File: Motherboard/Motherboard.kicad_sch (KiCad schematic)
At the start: 56 parts, among them J1 Conn_01x01, J10 ATX-24, J11 USB_B, J12 Bus_ISA_8bit, J13 65SIB_Connector, J2 Conn_01x01, J3 Conn_01x01, J4 Conn_01x01, J5 Conn_01x01, J6 Conn_01x01, J7 Conn_01x01, J8 Conn_01x01, J9 Bus_ISA_8bit, SW1 SW_Push, SW2 SW_SPST, U1 SC28L91, U10 XCR3064XL-VQ100, U11 XCR3064-VQ100, U12 LM7905_TO220, U13 MCP2200-I-SO, U14 74HCT163, U15 74HCT137, U2 AS6C1608, U3 WD65C22, U4 SST39SF040, U5 SST39SF040, U6 WD65C816S, U7 DS1813, U8 74HCT245, U9 74HCT573, X1 ACO-3.6864MHz, X2 ACO-24MHz, X3 ACO-14.31818MHz

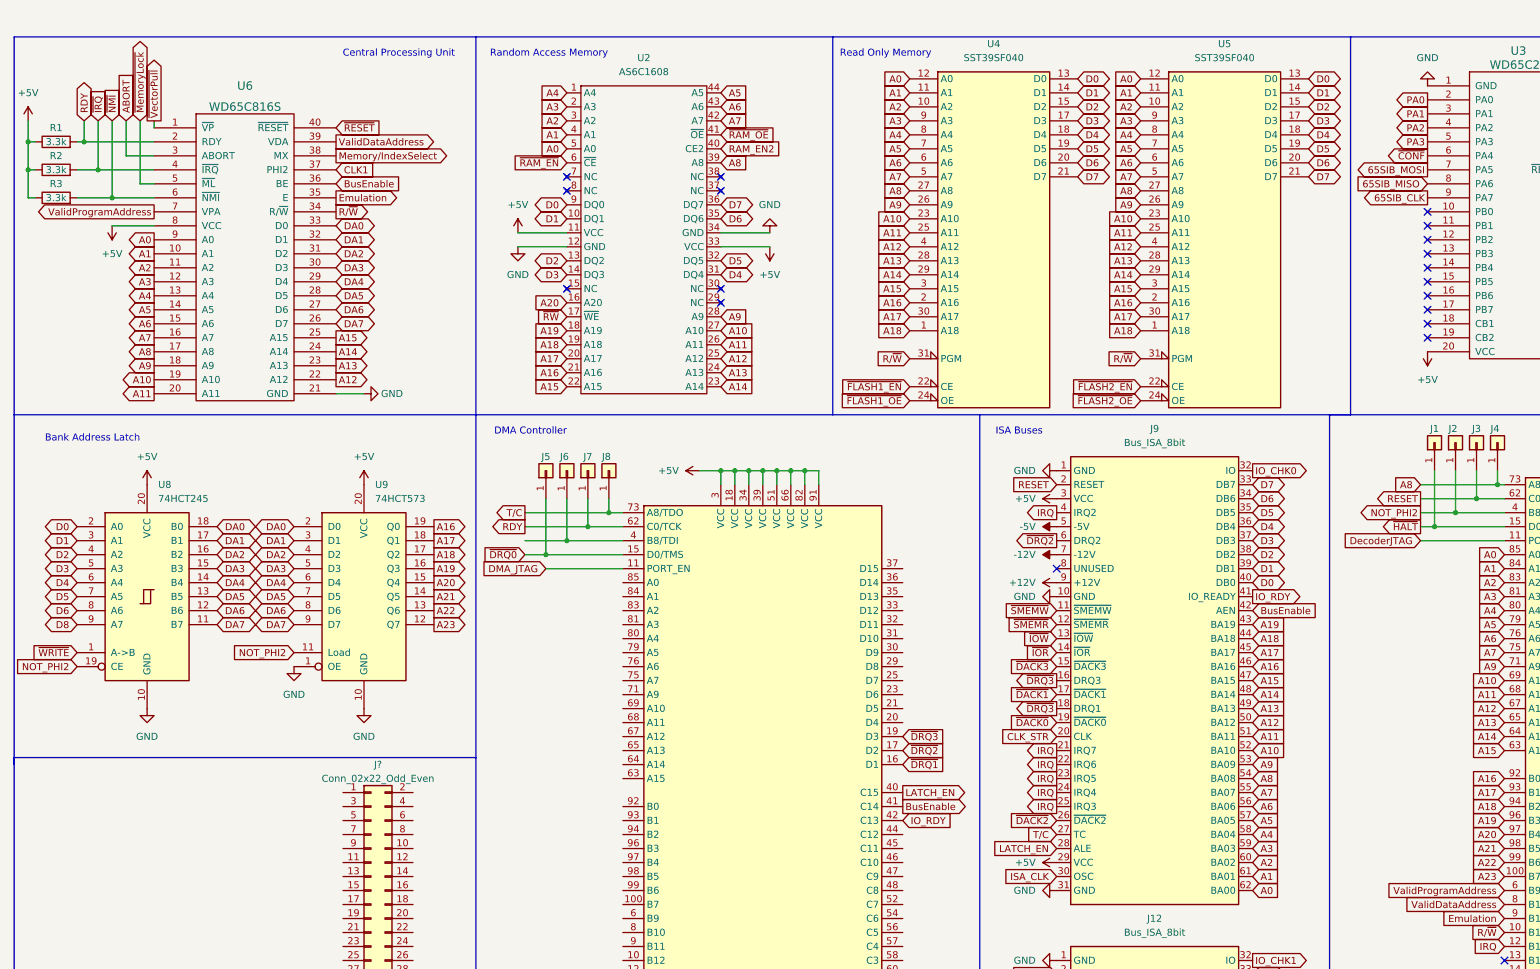
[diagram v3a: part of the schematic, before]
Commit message: Update Motherboard.kicad_sch
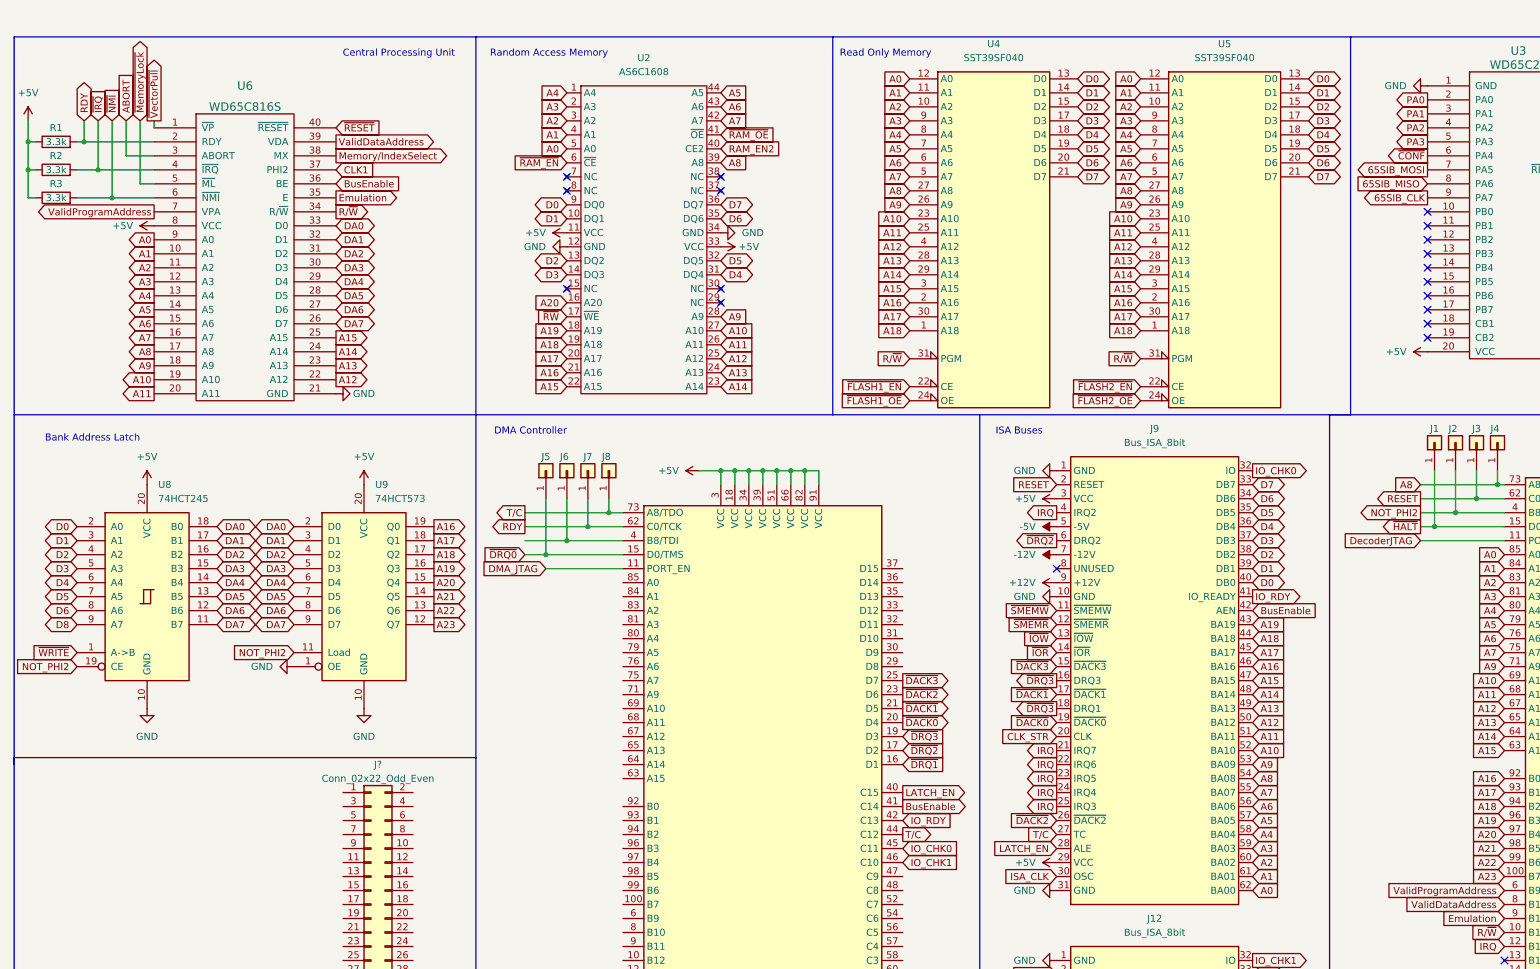
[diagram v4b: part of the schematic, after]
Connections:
- net IO_CHK0: now also U11.45 (C11)
- net IO_CHK1: now also U11.46 (C10)
- net T/C: now also U11.44 (C12)
- net ~{DACK0}: now also U11.20 (D4)
- net ~{DACK1}: now also U11.21 (D5)
- net ~{DACK2}: now also U11.23 (D6)
- net ~{DACK3}: now also U11.25 (D7)

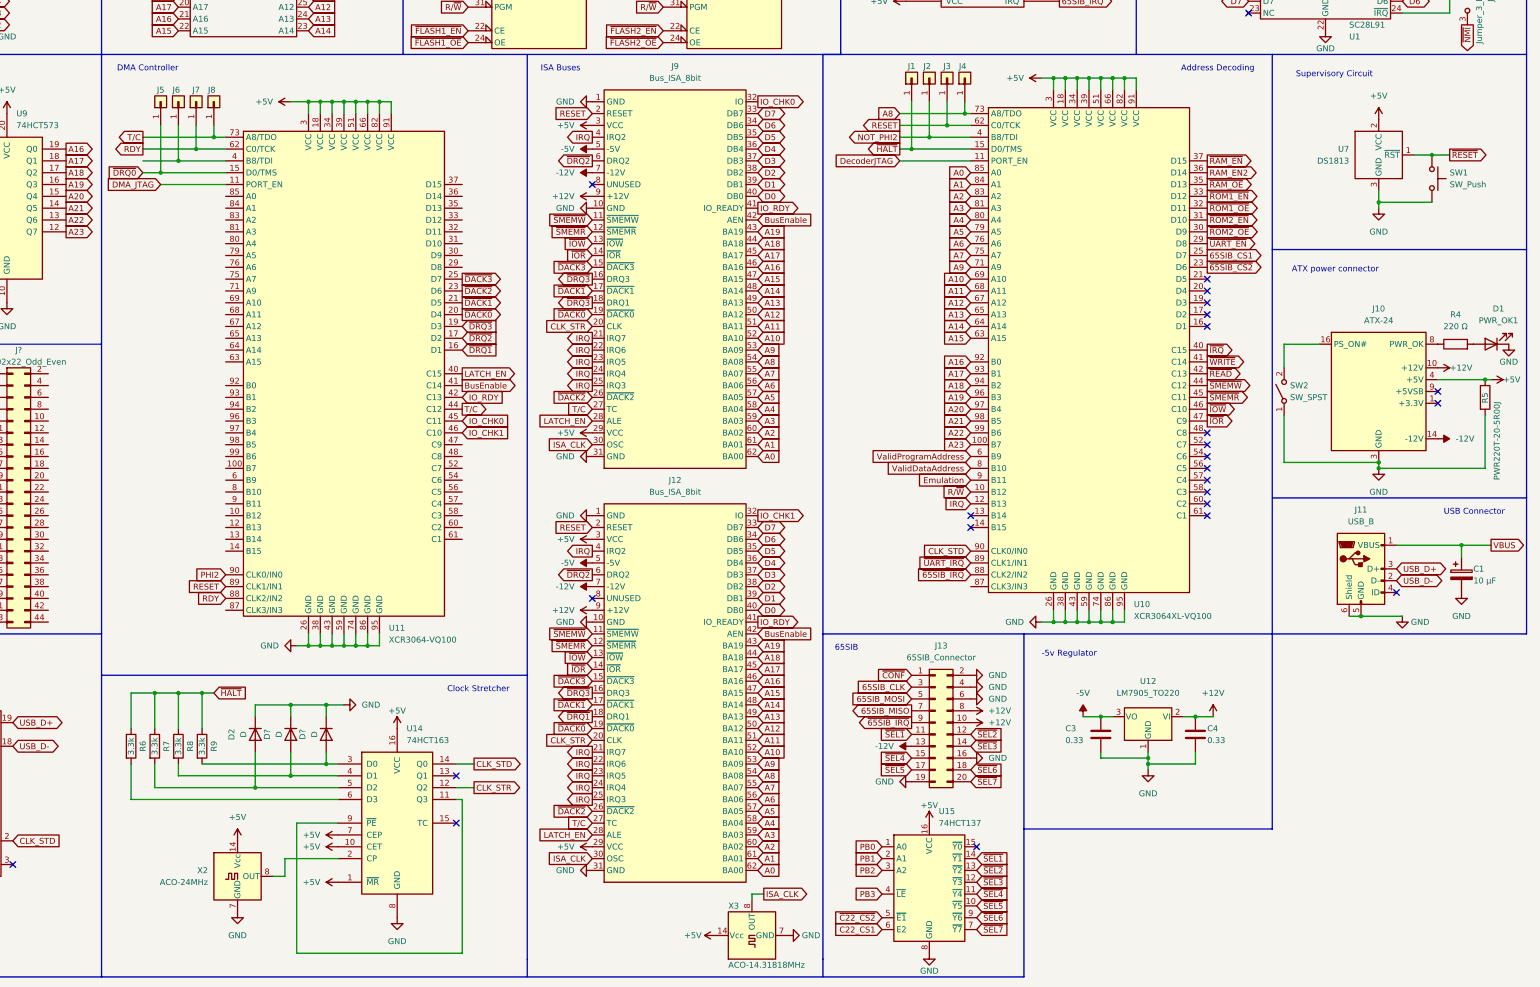
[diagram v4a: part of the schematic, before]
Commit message: Update Motherboard.kicad_sch
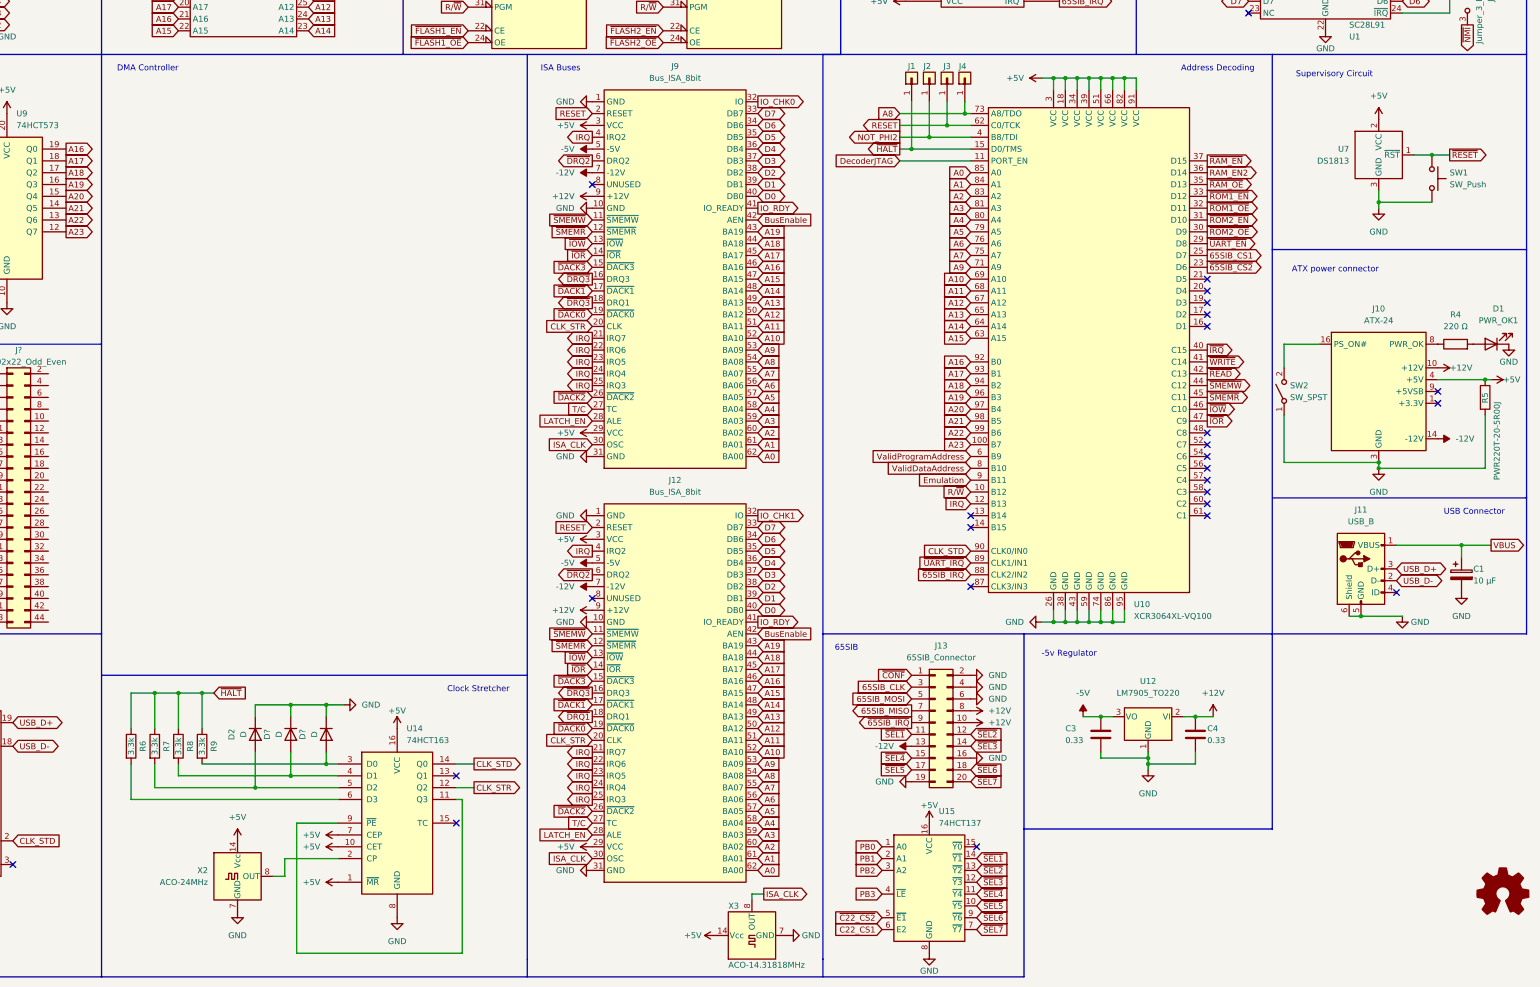
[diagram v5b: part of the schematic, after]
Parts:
- removed J5, J6, J7, J8: Conn_01x01, Connector_Pin:Pin_D1.0mm_L10.0mm, symbol Connector_Generic:Conn_01x01
- removed U11: XCR3064-VQ100, Package_QFP:LQFP-100_14x14mm_P0.5mm, symbol CPLD_Xilinx:XCR3064-VQ100
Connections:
- no-connect marks 70 -> 71

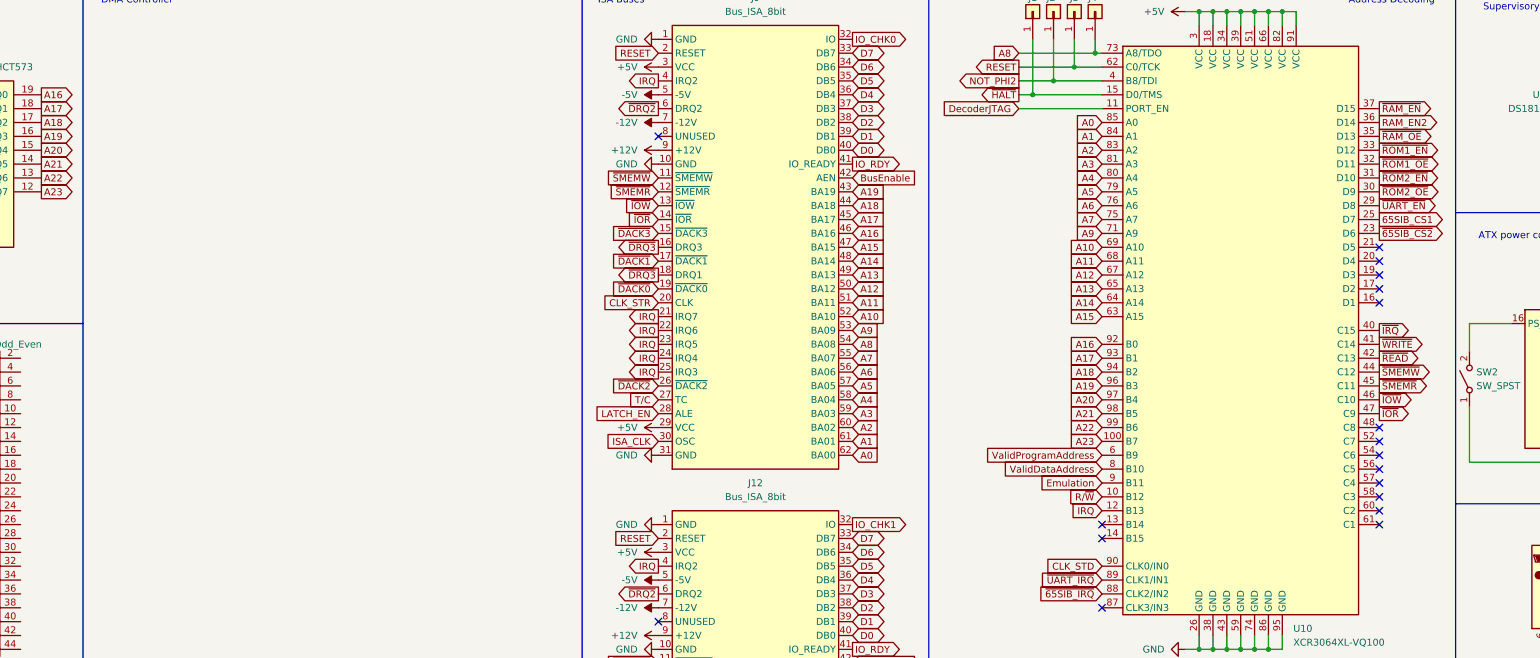
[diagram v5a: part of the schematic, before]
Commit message: Update Motherboard.kicad_sch
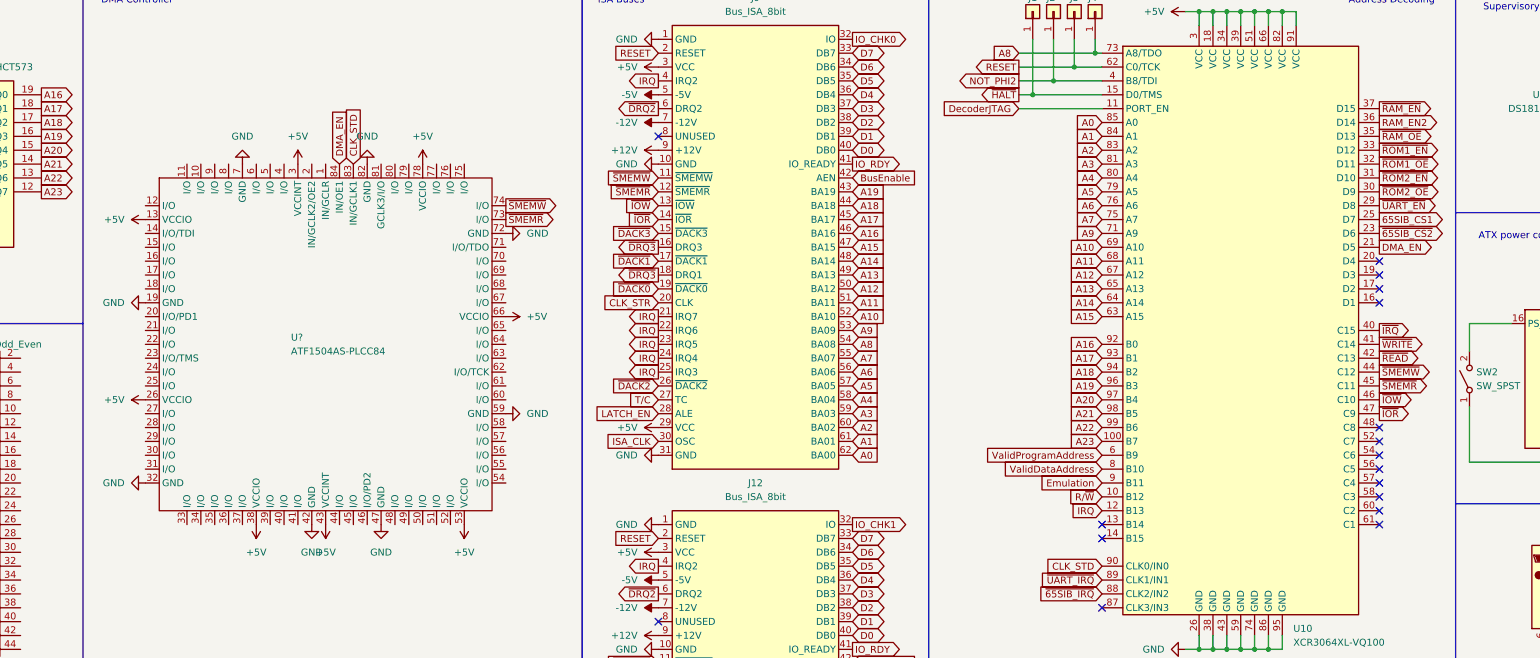
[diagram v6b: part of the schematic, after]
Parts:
- added U?: ATF1504AS-PLCC84, symbol CPLD:ATF1504AS-PLCC84
- J10: footprint (none) -> Connector_Molex:Molex_Mini-Fit_Jr_5569-24A2_2x12_P4.20mm_Horizontal
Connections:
- net +5V: now also U?.13 (VCCIO), U?.26 (VCCIO), U?.3 (VCCINT), U?.38 (VCCIO), U?.43 (VCCINT), U?.53 (VCCIO), U?.66 (VCCIO), U?.78 (VCCIO)
- net CLK_STD: now also U?.83 (IN/GCLK1)
- net GND: now also U?.19 (GND), U?.32 (GND), U?.42 (GND), U?.47 (GND), U?.59 (GND), U?.7 (GND), U?.72 (GND), U?.82 (GND)
- net ~{SMEMR}: now also U?.73 (I/O)
- net ~{SMEMW}: now also U?.74 (I/O)
- net DMA_EN: now reaches U10.21 (D5)
- net DMA_EN: now also U?.84 (IN/OE1)
- no-connect marks 71 -> 70
